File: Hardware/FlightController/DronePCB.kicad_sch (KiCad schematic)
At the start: 15 parts, among them U1 ESP32-DEVKIT-V1

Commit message: PCB Drone et manette finis avec gerbers générés
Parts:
- NRF24L01: footprint Connector_PinHeader_2.00mm:PinHeader_2x04_P2.00mm_Vertical -> Connector_PinHeader_2.54mm:PinHeader_2x04_P2.54mm_Vertical
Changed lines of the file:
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@@
 			)
 		)
-		(property "Footprint" "Connector_PinHeader_2.00mm:PinHeader_2x04_P2.00mm_Vertical"
+		(property "Footprint" "Connector_PinHeader_2.54mm:PinHeader_2x04_P2.54mm_Vertical"
 			(at 121.92 143.51 0)
 			(effects

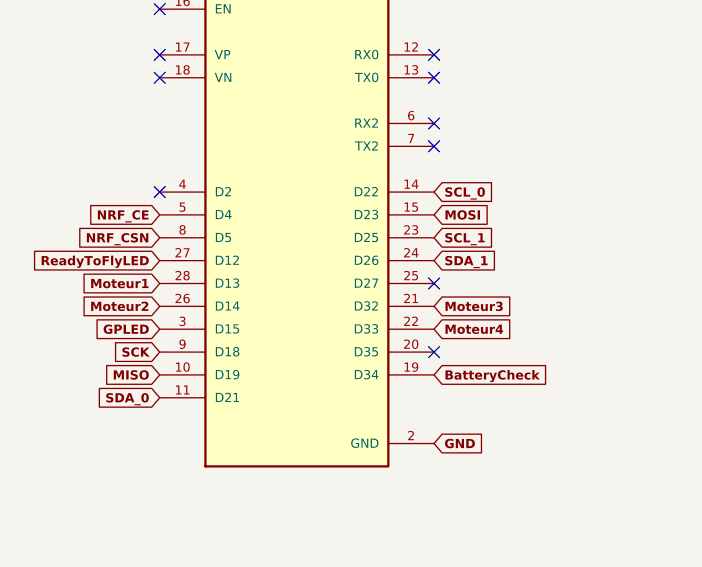
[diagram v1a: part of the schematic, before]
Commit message: Correction Drone pinout et génération gerber
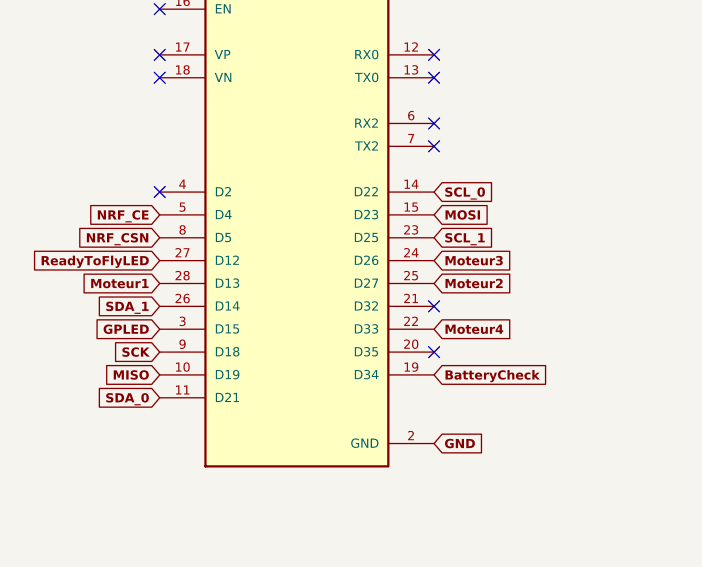
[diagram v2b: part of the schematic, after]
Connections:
- net Moteur2: now also U1.25 (D27); no longer U1.26 (D14)
- net Moteur3: now also U1.24 (D26); no longer U1.21 (D32)
- net SDA_1: now also U1.26 (D14); no longer U1.24 (D26)

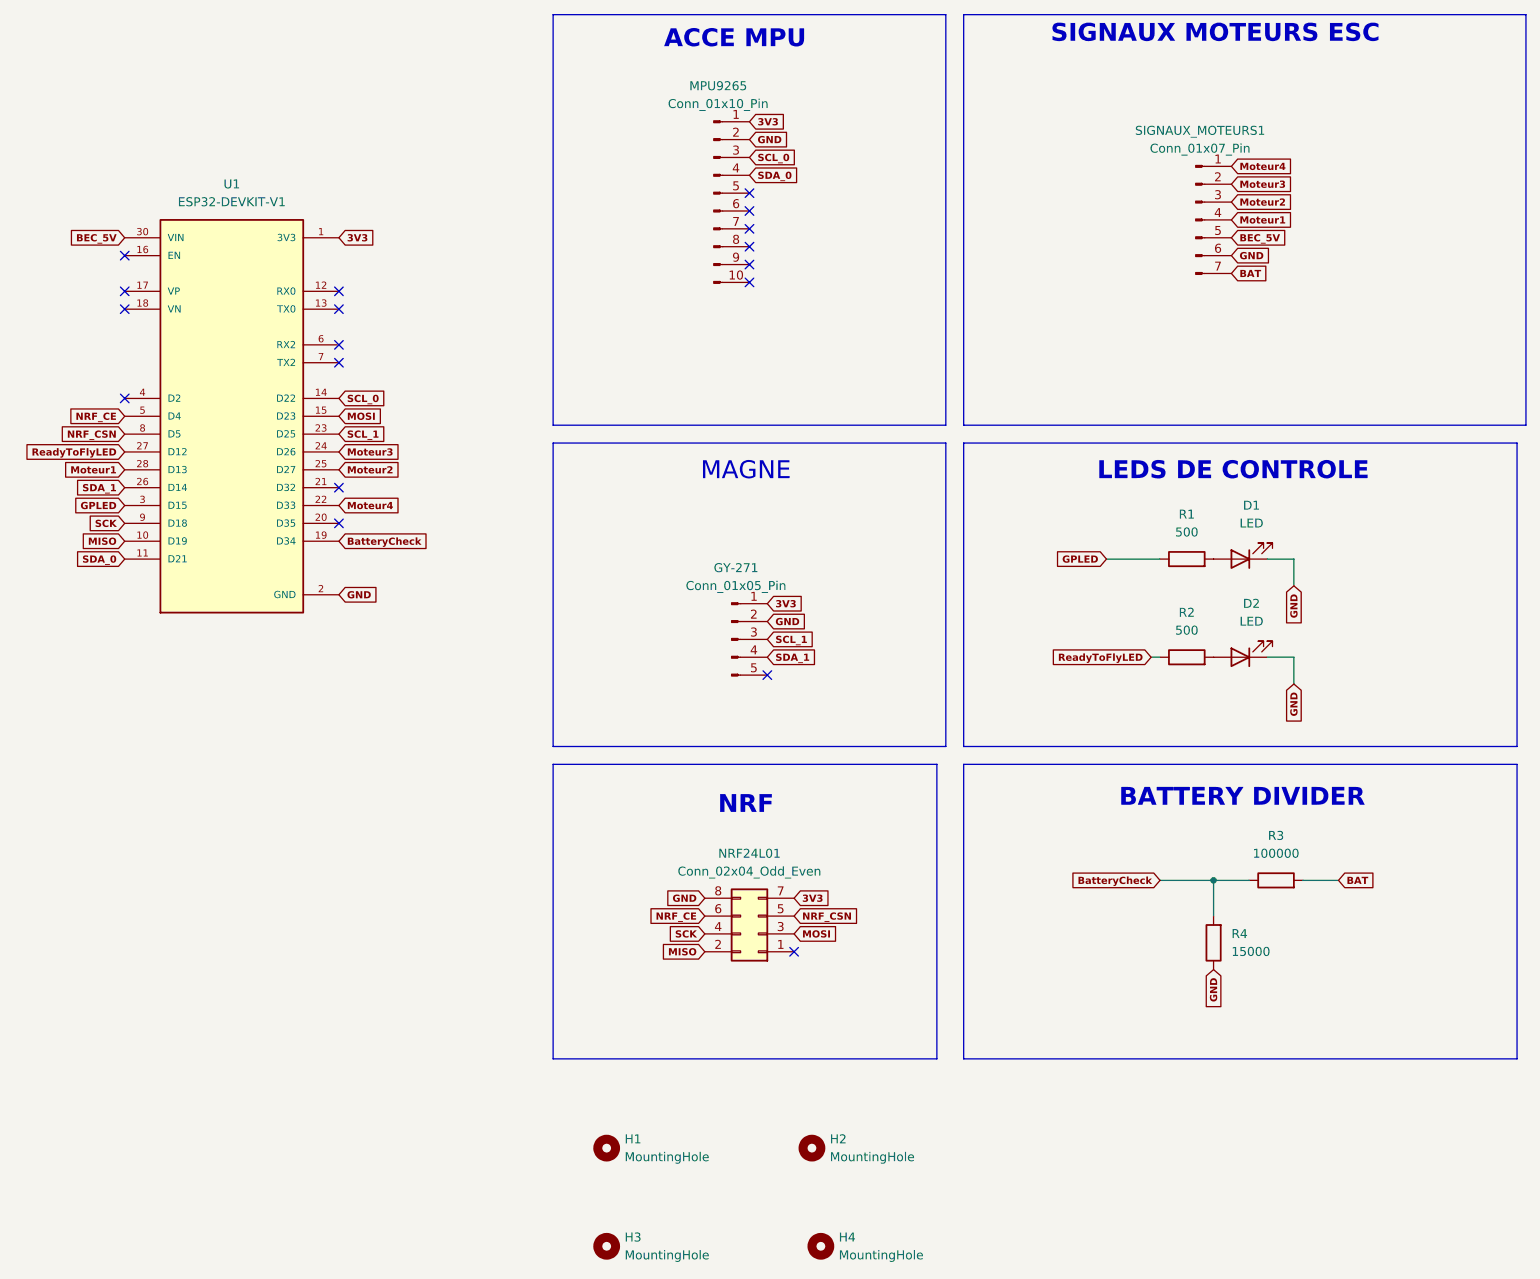
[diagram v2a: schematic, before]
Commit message: PCB avec nouveau connecteur JST SH + buffer
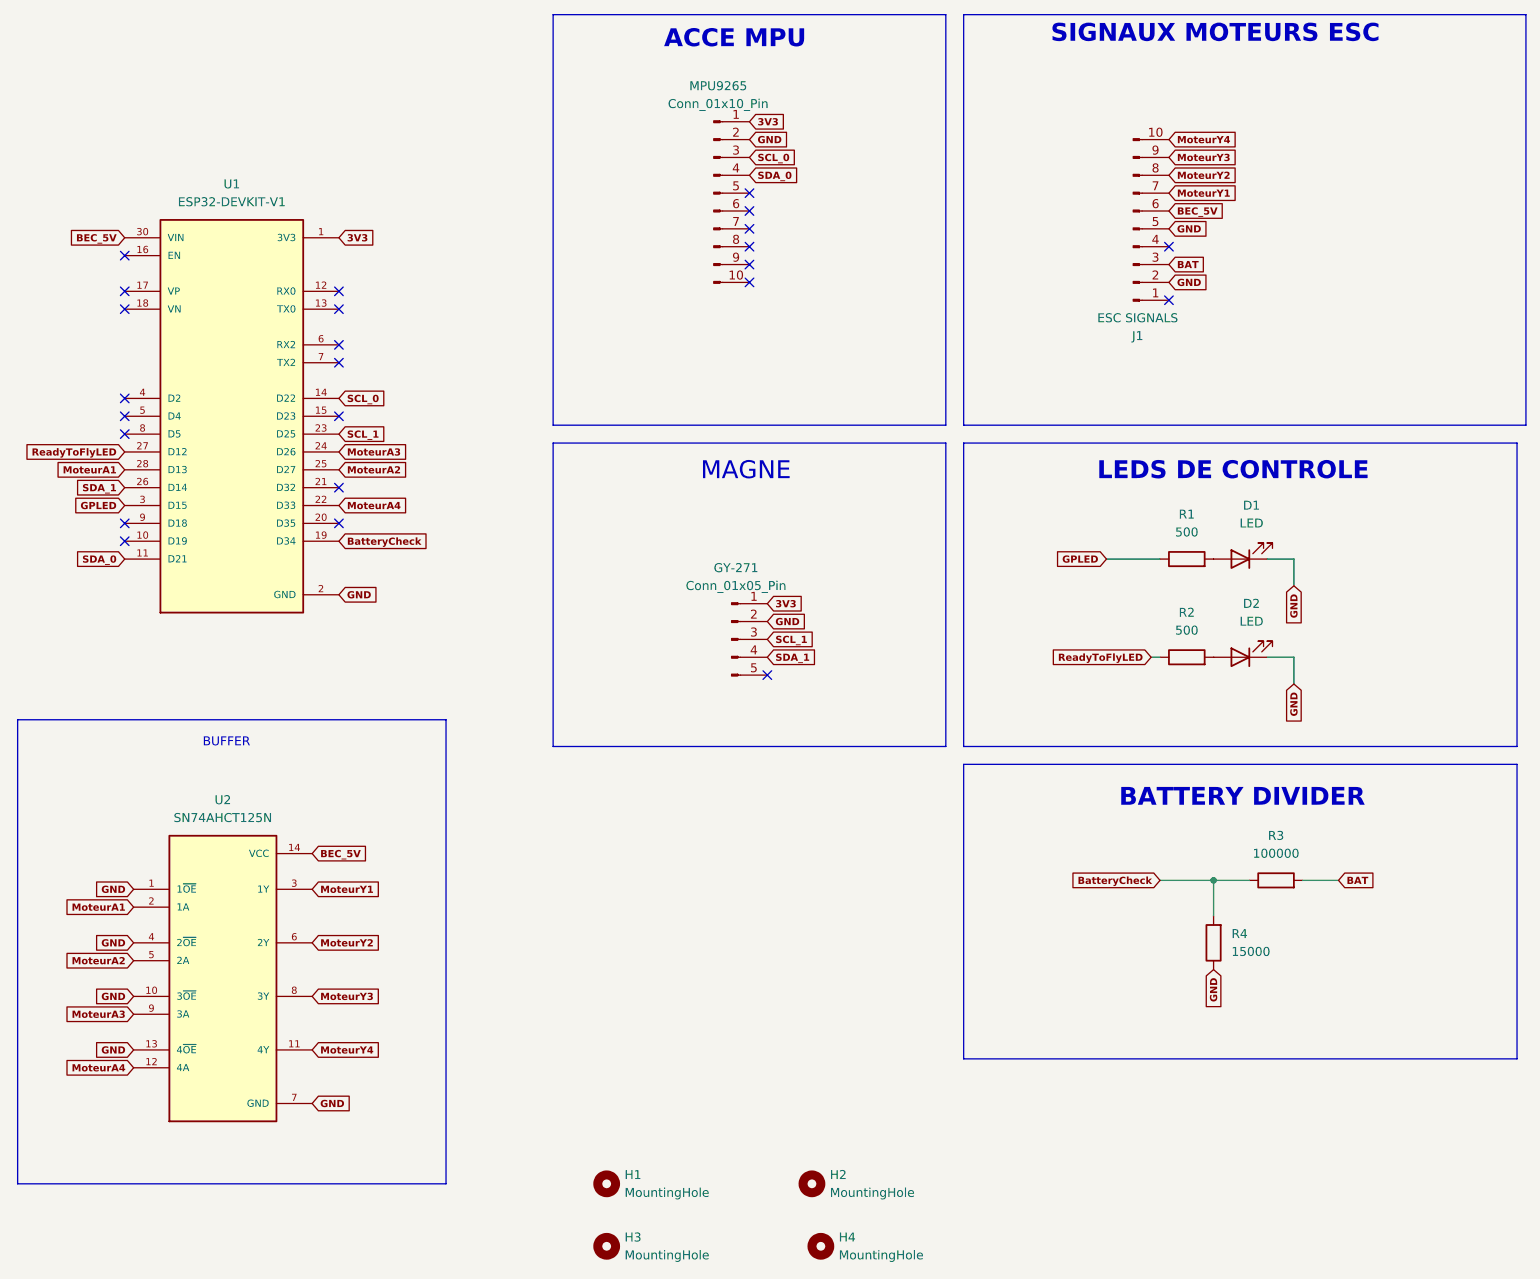
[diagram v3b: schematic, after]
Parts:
- removed NRF24L01: Conn_02x04_Odd_Even, Connector_PinHeader_2.54mm:PinHeader_2x04_P2.54mm_Vertical, symbol Connector_Generic:Conn_02x04_Odd_Even
- removed SIGNAUX_MOTEURS1: Conn_01x07_Pin, Connector_PinHeader_2.54mm:PinHeader_1x07_P2.54mm_Vertical, symbol Connector:Conn_01x07_Pin
- added J1: ESC SIGNALS, Connector_JST:JST_SHL_SM10B-SHLS-TF_1x10-1MP_P1.00mm_Horizontal, symbol Connector:Conn_01x10_Pin
- added U2: SN74AHCT125N, SN74AHCT125N_FP:DIP794W45P254L1930H508Q14, symbol SN74AHCT125N:SN74AHCT125N
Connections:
- net BAT: now also J1.3 (Pin_3)
- net BEC_5V: now also J1.6 (Pin_6), U2.14 (VCC)
- net GND: now also J1.2 (Pin_2), J1.5 (Pin_5), U2.1 (1~{OE}), U2.10 (3~{OE}), U2.13 (4~{OE}), U2.4 (2~{OE}), U2.7 (GND)
- net MISO: no longer names the net of U1.10 (D19)
- net MOSI: no longer names the net of U1.15 (D23)
- net Moteur1 renamed MoteurA1
- net MoteurA1: now also U2.2 (1A)
- net Moteur2 renamed MoteurA2
- net MoteurA2: now also U2.5 (2A)
- net Moteur3 renamed MoteurA3
- net MoteurA3: now also U2.9 (3A)
- net Moteur4 renamed MoteurA4
- net MoteurA4: now also U2.12 (4A)
- net NRF_CE: no longer names the net of U1.5 (D4)
- net NRF_CSN: no longer names the net of U1.8 (D5)
- net SCK: no longer names the net of U1.9 (D18)
- new net MoteurY1: J1.7 (Pin_7), U2.3 (1Y)
- new net MoteurY2: J1.8 (Pin_8), U2.6 (2Y)
- new net MoteurY3: J1.9 (Pin_9), U2.8 (3Y)
- new net MoteurY4: J1.10 (Pin_10), U2.11 (4Y)
- no-connect marks 18 -> 24
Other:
- note added: "BUFFER"
- note removed: "NRF"
- moved on the sheet: H1, H2
